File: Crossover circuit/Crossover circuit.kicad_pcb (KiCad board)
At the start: 2 copper layers, 124.5 x 102.9 mm, 31 parts, among them J1 OSTTC020162, J2 OSTTC020162, J3 OSTTC020162

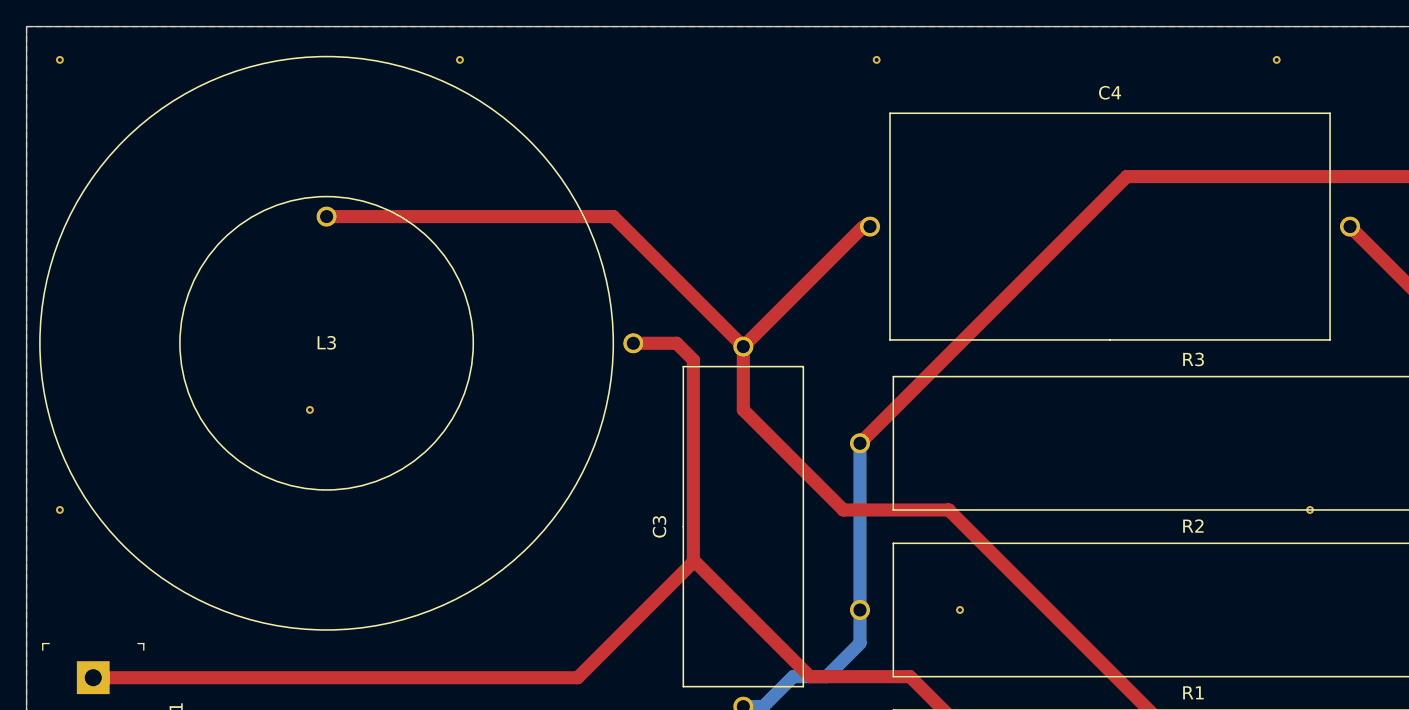
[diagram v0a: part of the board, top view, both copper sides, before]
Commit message: Fixed issue where L3 was flipped on the x-axis
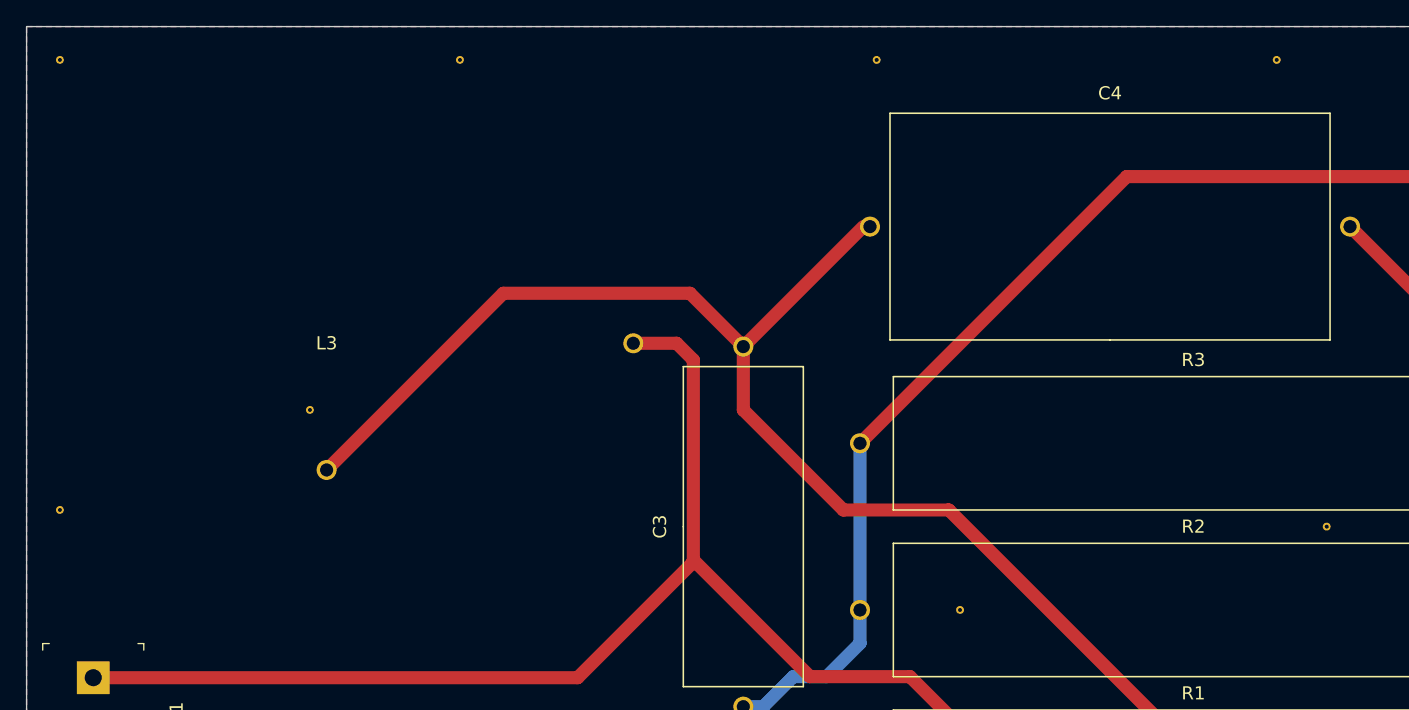
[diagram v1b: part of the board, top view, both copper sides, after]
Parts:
- L3: moved to B.Cu
- moved REF** 1.80 mm to (176.5, 78.7)
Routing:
- net Net-(C3-Pad2): track 145.6 -> 148.8 mm
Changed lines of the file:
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@@
     (thickness 1.6)
     (drawings 9)
-    (tracks 64)
+    (tracks 65)
     (zones 0)
     (modules 31)
@@
     (solder_mask_min_width 0.25)
     (aux_axis_origin 0 0)
-    (visible_elements FFFFFF7F)
+    (visible_elements 7FFFFFFF)
     (pcbplotparams
       (layerselection 0x010fc_ffffffff)
@@
   )
   (module Crossover:Via (layer F.Cu)
-    (at 175.26 77.47)
+    (at 176.53 78.74)
     (fp_text reference REF** (at 0 -3.048) (layer F.SilkS) hide
       (effects (font (size 1 1) (thickness 0.15)))
@@
       (zone_connect 2))
   )
-  (module "Crossover:1.2 mH inductor" (layer F.Cu)
+  (module "Crossover:1.2 mH inductor" (layer B.Cu)
     (at 100.33 64.77)
     (fp_text reference L3 (at 0 0) (layer F.SilkS)
       (effects (font (size 1 1) (thickness 0.15)))
     )
-    (fp_text value "1.2 mH" (at 0 -22.86) (layer F.Fab)
-      (effects (font (size 1 1) (thickness 0.15)))
-    )
-    (fp_circle (center 0 0) (end 0 -11.176) (layer F.SilkS) (width 0.12))
-    (fp_circle (center 0 0) (end 0 21.844) (layer F.SilkS) (width 0.12))
-    (pad 2 thru_hole circle (at 0 -9.652) (size 1.524 1.524) (drill 1) (layers *.Cu *.Mask)
-      (net 4 "Net-(C3-Pad2)"))
+    (fp_text value "1.2 mH" (at 0 22.86) (layer B.Fab)
+      (effects (font (size 1 1) (thickness 0.15)) (justify mirror))
+    )
+    (fp_circle (center 0 0) (end 0 -21.844) (layer B.SilkS) (width 0.12))
+    (fp_circle (center 0 0) (end 0 11.176) (layer B.SilkS) (width 0.12))
     (pad 1 thru_hole circle (at 23.368 0) (size 1.524 1.524) (drill 1) (layers *.Cu *.Mask)
       (net 2 "Net-(C1-Pad1)"))
+    (pad 2 thru_hole circle (at 0 9.652) (size 1.524 1.524) (drill 1) (layers *.Cu *.Mask)
+      (net 4 "Net-(C3-Pad2)"))
   )
   (module digikey-footprints:Term_Block_1x2_P5mm (layer F.Cu)
@@
   (segment (start 141.224 55.88) (end 141.732 55.88) (width 0.25) (layer F.Cu) (net 4))
   (segment (start 132.08 65.024) (end 141.224 55.88) (width 1) (layer F.Cu) (net 4))
-  (segment (start 122.174 55.118) (end 132.08 65.024) (width 1) (layer F.Cu) (net 4))
-  (segment (start 100.33 55.118) (end 122.174 55.118) (width 1) (layer F.Cu) (net 4))
   (segment (start 147.737766 77.47) (end 139.7 77.47) (width 1) (layer F.Cu) (net 4))
   (segment (start 132.08 69.85) (end 132.08 65.024) (width 1) (layer F.Cu) (net 4))
@@
   (segment (start 196.85 129.62) (end 196.85 127) (width 1) (layer F.Cu) (net 4))
   (segment (start 197.058883 126.791117) (end 147.737766 77.47) (width 1) (layer F.Cu) (net 4))
+  (segment (start 113.792 60.96) (end 100.33 74.422) (width 1) (layer F.Cu) (net 4))
+  (segment (start 132.08 65.024) (end 128.016 60.96) (width 1) (layer F.Cu) (net 4))
+  (segment (start 128.016 60.96) (end 113.792 60.96) (width 1) (layer F.Cu) (net 4))
   (segment (start 190.754 140.716) (end 188.722 140.716) (width 1) (layer F.Cu) (net 5))
   (segment (start 191.77 139.7) (end 190.754 140.716) (width 1) (layer F.Cu) (net 5))

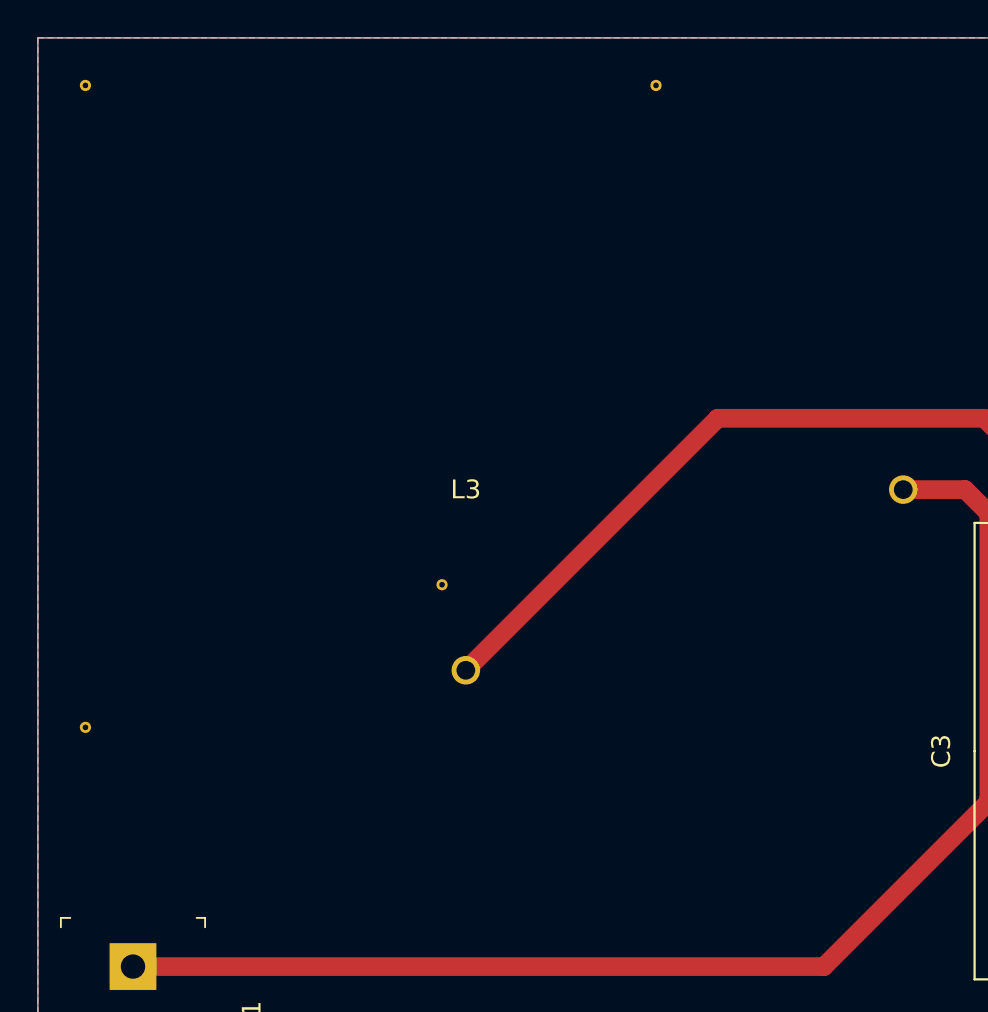
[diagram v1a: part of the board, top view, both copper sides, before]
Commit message: flipping an inductor's footprint
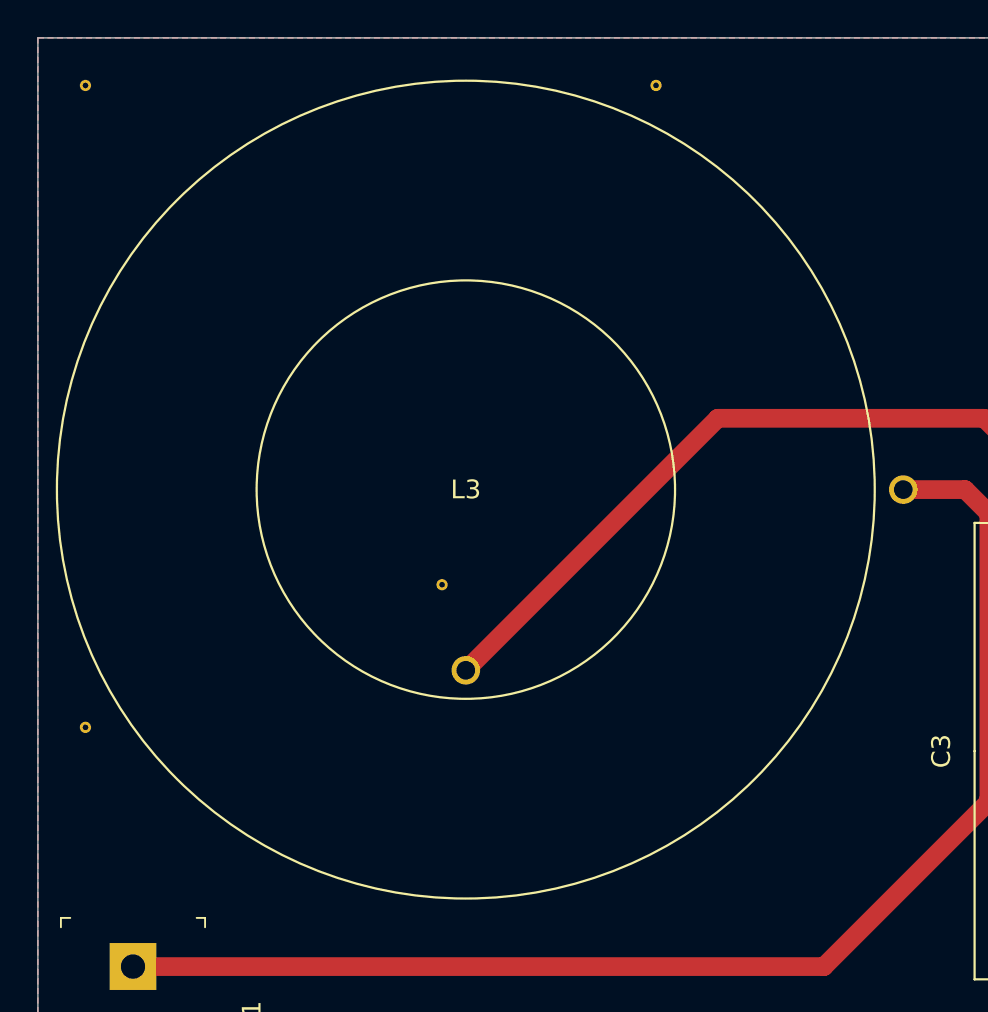
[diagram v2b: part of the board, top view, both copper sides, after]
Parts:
- L3: moved to F.Cu
